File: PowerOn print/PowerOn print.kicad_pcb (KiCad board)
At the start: 2 copper layers, 0.8 x 0.7 mm, 10 parts, among them J1 USB4140-GF-0230-C_REV04, J2 USB4140-GF-0230-C_REV04, J3 Conn_01x05_Male, J4 Conn_01x02_Male, Q1 IRF7404, Q2 MMBT3904

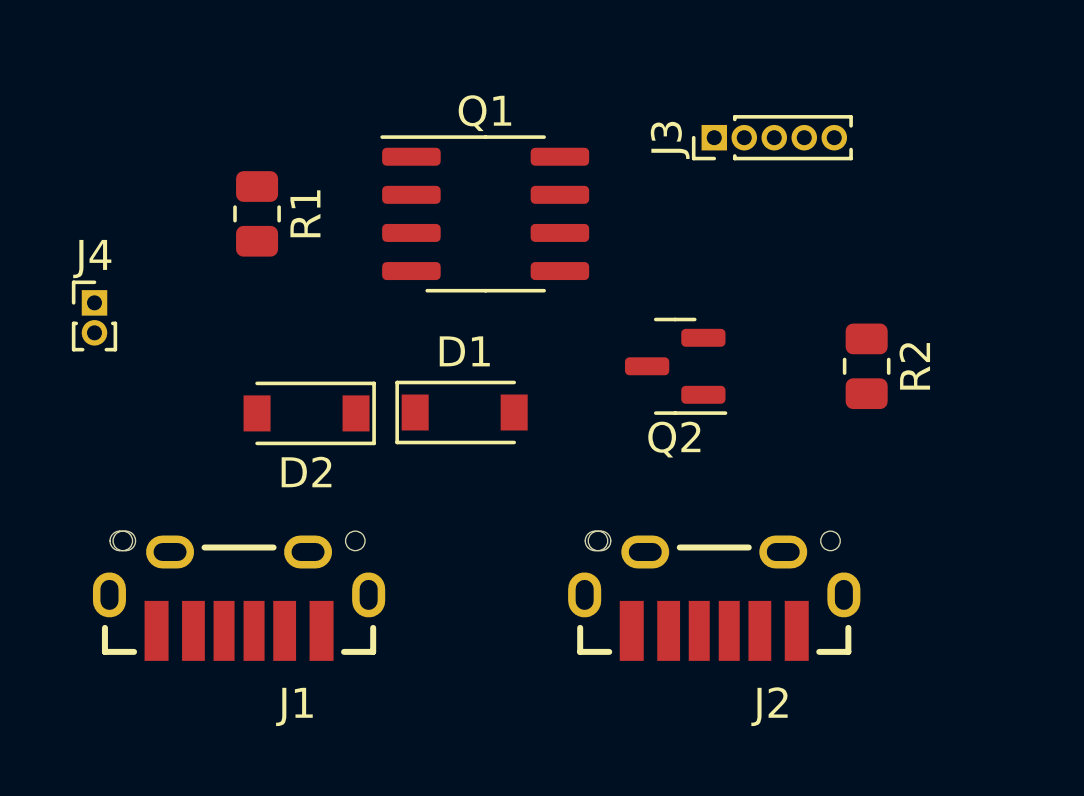
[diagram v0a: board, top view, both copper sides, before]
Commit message: PCB-Poweron-print-only
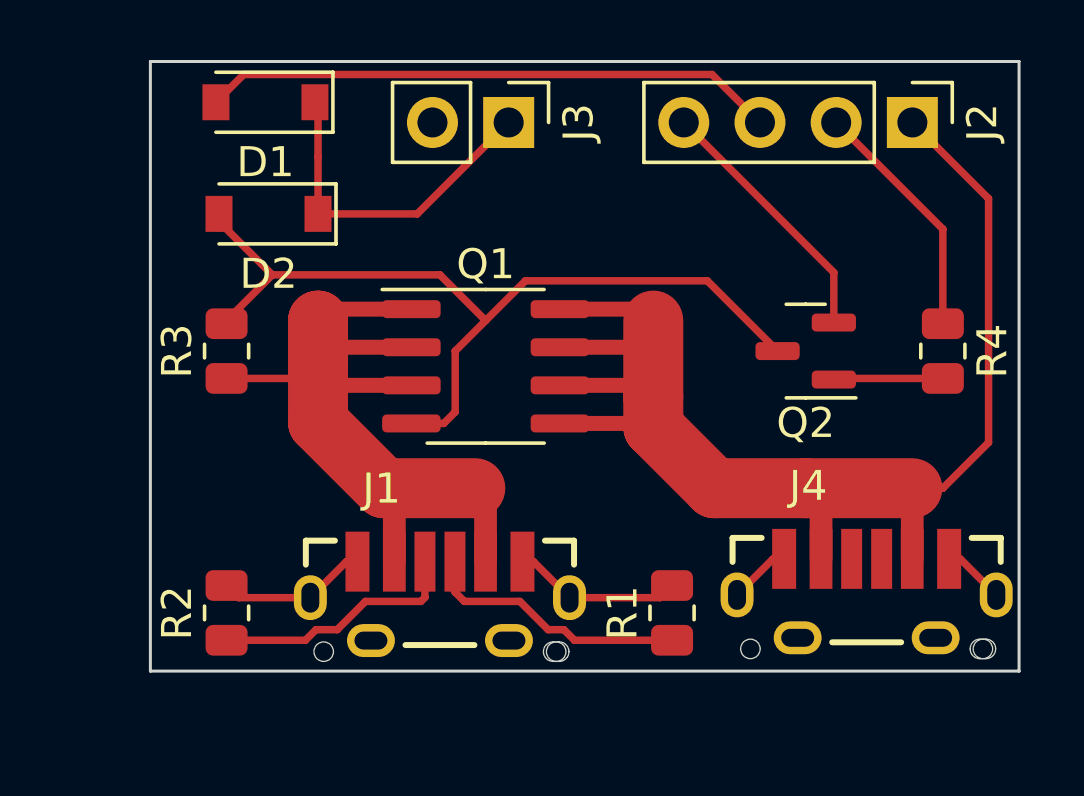
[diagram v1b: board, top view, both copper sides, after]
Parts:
- removed the J3 at (127.0, 68.6)
- added J4: USB4140-GF-0230-C_REV0.4, USB4140-GF-0230-C_REV0:GCT_USB4140-GF-0230-C_REV0.4, F.Cu at (132.1, 83.8)
- added R1: 5k1, Resistor_SMD:R_0805_2012Metric, F.Cu at (125.6, 84.4)
- added R2: 5k1, Resistor_SMD:R_0805_2012Metric, F.Cu at (110.7, 84.4)
- J1: value USB4140-GF-0230-C_REV04 -> USB4140-GF-0230-C_REV0.4; footprint Connector_USB:GCT_USB4140-GF-0230-C_REV0.4 -> USB4140-GF-0230-C_REV0:GCT_USB4140-GF-0230-C_REV0.4
- J2: value USB4140-GF-0230-C_REV04 -> Conn_01x04_Male; footprint Connector_USB:GCT_USB4140-GF-0230-C_REV0.4 -> Connector_PinHeader_2.54mm:PinHeader_1x04_P2.54mm_Vertical
- J3: renamed from J4; footprint Connector_PinHeader_1.00mm:PinHeader_1x02_P1.00mm_Vertical -> Connector_PinHeader_2.54mm:PinHeader_1x02_P2.54mm_Vertical
- moved J2 17.1 mm to (133.6, 68.1), turned to -90 degrees
- moved J3 15.1 mm to (120.1, 68.1), turned to -90 degrees
- moved D1 12.3 mm to (112.0, 67.4), turned to 180 degrees
- moved D2 6.77 mm to (112.1, 71.1)
- moved J1 6.70 mm to (117.9, 83.9), turned to 0 degrees
- moved Q1 5.08 mm to (119.4, 76.2)
- moved R3 4.68 mm to (110.7, 75.7), turned to 90 degrees
- moved Q2 4.38 mm to (130.0, 75.7)
- moved R4 2.59 mm to (134.6, 75.7)
- renumbered R1 to R3, R2 to R4
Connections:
- net SW0 renamed Net-(D1-Pad1)
- J1 pad A12: SW1 -> GND
- J1 pad A5: Net-(J2-PadA5) -> Net-(J1-PadA5)
- J1 pad B12: SW1 -> GND
- J1 pad B5: Net-(J2-PadB5) -> Net-(J1-PadB5)
- J1 pad S1: SW1 -> GND
- J1 pad S2: SW1 -> GND
- J1 pad S3: SW1 -> GND
- J1 pad S4: SW1 -> GND
- J3 pad 2: SW1 -> GND
- Q1 pad 5: Battery probe -> +5V
- Q1 pad 6: Battery probe -> +5V
- Q1 pad 7: Battery probe -> +5V
- Q1 pad 8: Battery probe -> +5V
- Q2 pad 2: SW1 -> GND
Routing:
- net +5V: track 0.00 -> 46.4 mm
- net Net-(D2-Pad2): track 0.00 -> 29.9 mm
- net Net-(J1-PadA9): track 0.00 -> 29.5 mm
- net GND: track 0.00 -> 23.6 mm
- net GPIO1: track 0.00 -> 19.2 mm
- net Net-(D1-Pad1): track 0.00 -> 11.5 mm
- net Net-(J1-PadB5): track 0.00 -> 8.91 mm
- net Net-(J1-PadA5): track 0.00 -> 8.40 mm
- net GPIO0: track 0.00 -> 8.18 mm
- net Net-(Q2-Pad1): track 0.00 -> 3.65 mm
- added copper zone on B.Cu, net GND
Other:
- board size 0.8 x 0.7 mm -> 29 x 20.3 mm

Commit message: Poweron print adapted
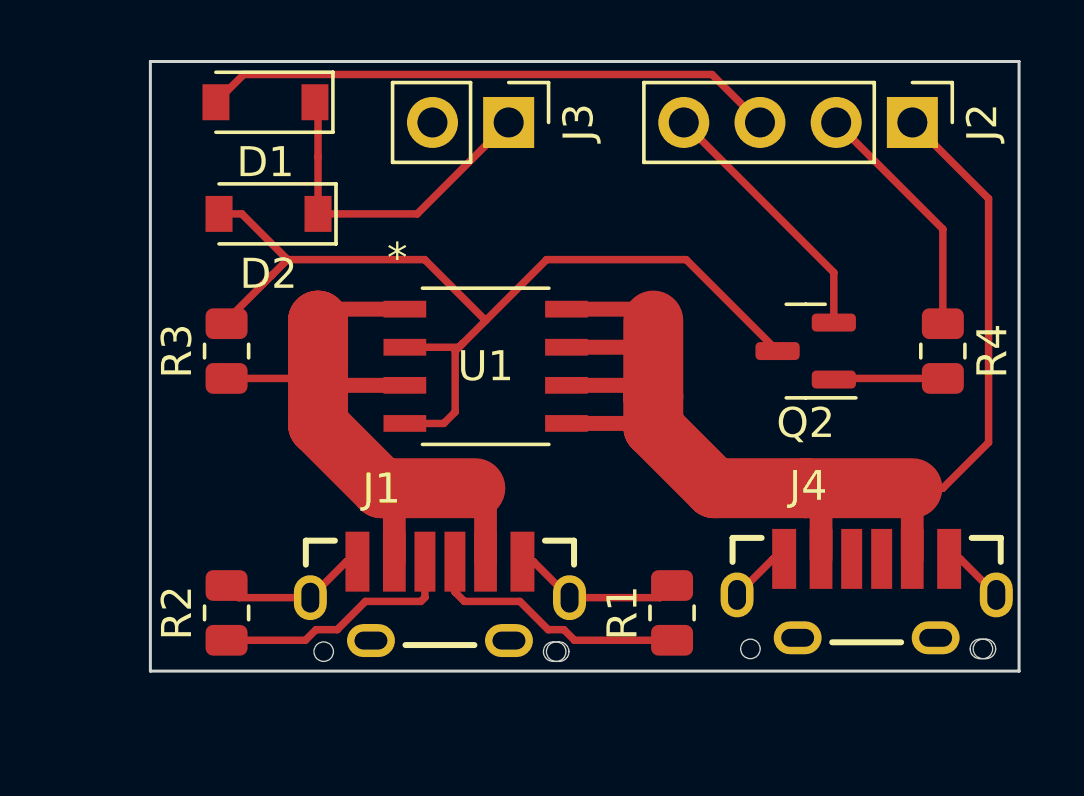
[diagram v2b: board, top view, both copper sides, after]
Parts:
- removed Q1: IRF7404, Package_SO:SOIC-8_3.9x4.9mm_P1.27mm
- added U1: DMP3028LSD-13, footprints:DMP3028LSD-13, F.Cu at (119.4, 76.2)
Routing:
- net Net-(J1-PadA9): track 29.5 -> 26.1 mm
- net Net-(D2-Pad2): track 29.9 -> 32.4 mm
- net +5V: track 46.4 -> 45.5 mm
